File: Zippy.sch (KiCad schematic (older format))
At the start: 0 parts

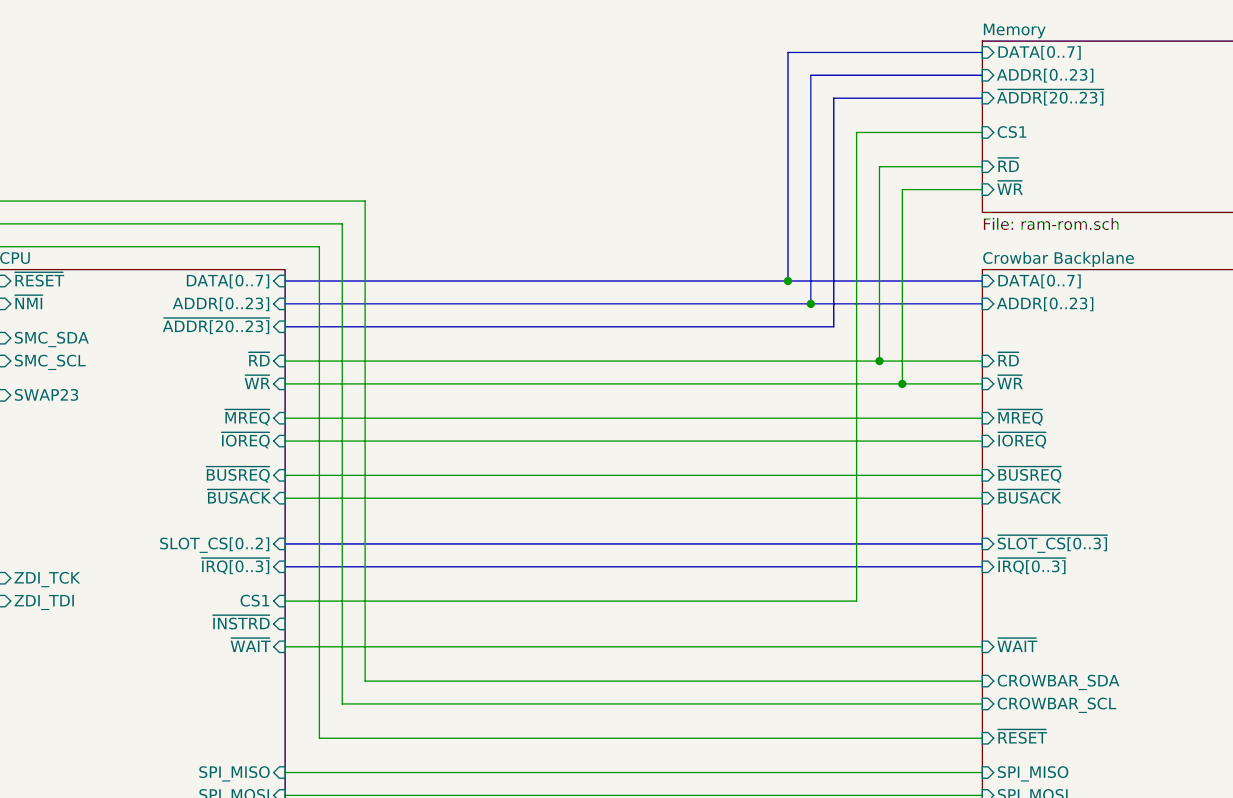
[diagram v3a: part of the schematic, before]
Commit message: boot rom: Add in the symbol for the Flash and integrate into the system   - Add the Flash ROM schematic symbol.   - Add to the ram-rom schematic.   - Get rid of /INSTRD -- not really useful.   - Export /CS0 so we can select the Flash ROM.
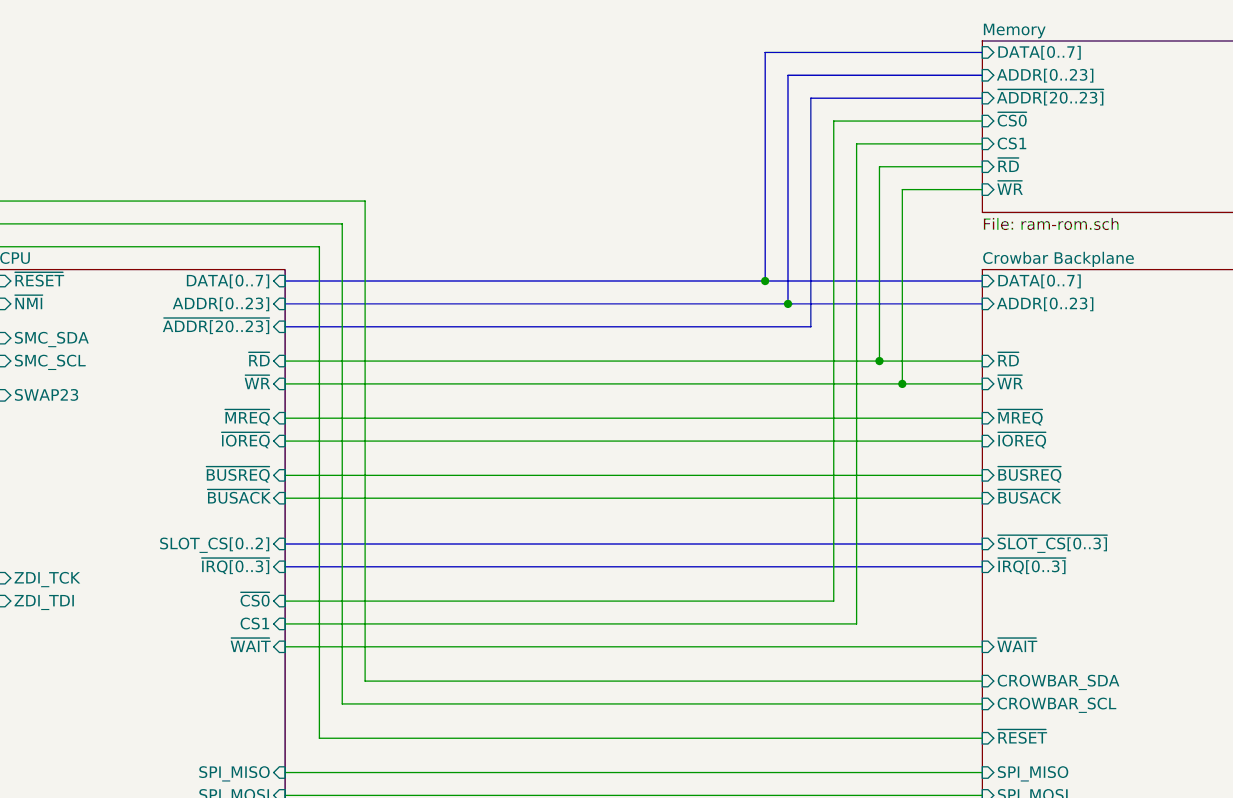
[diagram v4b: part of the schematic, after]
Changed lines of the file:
@@
 F4 "ADDR[0..23]" I R 6900 3000 50
 F5 "DATA[0..7]" I R 6900 2900 50
-F7 "ZDI_TCK" I L 5650 4200 50
-F8 "ZDI_TDI" I L 5650 4300 50
-F9 "~NMI" I L 5650 3000 50
-F10 "~IOREQ" I R 6900 3600 50
-F11 "~MREQ" I R 6900 3500 50
-F12 "~RD" I R 6900 3250 50
-F13 "~WR" I R 6900 3350 50
-F14 "~INSTRD" I R 6900 4400 50
-F15 "~WAIT" I R 6900 4500 50
-F16 "~BUSREQ" I R 6900 3750 50
-F17 "~BUSACK" I R 6900 3850 50
-F18 "SMC_SCL" I L 5650 3250 50
-F19 "SMC_SDA" I L 5650 3150 50
-F20 "SPI_SCLK" I R 6900 5250 50
-F21 "SPI_MISO" I R 6900 5050 50
-F22 "SPI_MOSI" I R 6900 5150 50
-F23 "SLOT_CS[0..2]" I R 6900 4050 50
-F24 "~ADDR[20..23]" I R 6900 3100 50
-F25 "~IRQ[0..3]" I R 6900 4150 50
-F26 "CS1" I R 6900 4300 50
-F27 "SWAP23" I L 5650 3400 50
-F28 "~SPI_SS[0..3]" I R 6900 5350 50
+F6 "ZDI_TCK" I L 5650 4200 50
+F7 "ZDI_TDI" I L 5650 4300 50
+F8 "~NMI" I L 5650 3000 50
+F9 "~IOREQ" I R 6900 3600 50
+F10 "~MREQ" I R 6900 3500 50
+F11 "~RD" I R 6900 3250 50
+F12 "~WR" I R 6900 3350 50
+F14 "~WAIT" I R 6900 4500 50
+F15 "~BUSREQ" I R 6900 3750 50
+F16 "~BUSACK" I R 6900 3850 50
+F17 "SMC_SCL" I L 5650 3250 50
+F18 "SMC_SDA" I L 5650 3150 50
+F19 "SPI_SCLK" I R 6900 5250 50
+F20 "SPI_MISO" I R 6900 5050 50
+F21 "SPI_MOSI" I R 6900 5150 50
+F22 "SLOT_CS[0..2]" I R 6900 4050 50
+F23 "~ADDR[20..23]" I R 6900 3100 50
+F24 "~IRQ[0..3]" I R 6900 4150 50
+F25 "CS1" I R 6900 4400 50
+F26 "SWAP23" I L 5650 3400 50
+F27 "~SPI_SS[0..3]" I R 6900 5350 50
+F28 "~CS0" I R 6900 4300 50
 $EndSheet
 $Sheet
@@
 F4 "~RD" I L 9950 2400 50
 F5 "~WR" I L 9950 2500 50
-F13 "~ADDR[20..23]" I L 9950 2100 50
-F14 "CS1" I L 9950 2250 50
+F6 "~ADDR[20..23]" I L 9950 2100 50
+F7 "CS1" I L 9950 2300 50
+F8 "~CS0" I L 9950 2200 50
 $EndSheet
 Wire Wire Line
 	5650 3400 4650 3400
 Wire Bus Line
-	6900 2900 9100 2900
-Wire Bus Line
-	6900 3000 9200 3000
+	6900 2900 9000 2900
+Wire Bus Line
+	6900 3000 9100 3000
 Wire Wire Line
 	6900 3250 9500 3250
@@
 	7250 4650 9950 4650
 Wire Wire Line
-	6900 4300 9400 4300
-Wire Wire Line
-	9400 4300 9400 2250
-Wire Wire Line
-	9400 2250 9950 2250
+	6900 4400 9400 4400
+Wire Wire Line
+	9400 4400 9400 2300
+Wire Wire Line
+	9400 2300 9950 2300
 Wire Wire Line
 	9500 3250 9500 2400
@@
 	9600 3350 6900 3350
 Wire Bus Line
-	6900 3100 9300 3100
-Wire Bus Line
-	9300 3100 9300 2100
-Wire Bus Line
-	9300 2100 9950 2100
-Wire Bus Line
-	9950 2000 9200 2000
-Wire Bus Line
-	9200 2000 9200 3000
-Connection ~ 9200 3000
-Wire Bus Line
-	9200 3000 9950 3000
-Wire Bus Line
-	9950 1900 9100 1900
-Wire Bus Line
-	9100 1900 9100 2900
-Connection ~ 9100 2900
-Wire Bus Line
-	9100 2900 9950 2900
+	6900 3100 9200 3100
+Wire Bus Line
+	9200 3100 9200 2100
+Wire Bus Line
+	9200 2100 9950 2100
+Wire Bus Line
+	9950 2000 9100 2000
+Wire Bus Line
+	9100 2000 9100 3000
+Connection ~ 9100 3000
+Wire Bus Line
+	9100 3000 9950 3000
+Wire Bus Line
+	9950 1900 9000 1900
+Wire Bus Line
+	9000 1900 9000 2900
+Connection ~ 9000 2900
+Wire Bus Line
+	9000 2900 9950 2900
 Wire Wire Line
 	6900 5850 9950 5850
@@
 Wire Wire Line
 	4650 2550 7250 2550
+Wire Wire Line
+	6900 4300 9300 4300
+Wire Wire Line
+	9300 4300 9300 2200
+Wire Wire Line
+	9300 2200 9950 2200
 $EndSCHEMATC
